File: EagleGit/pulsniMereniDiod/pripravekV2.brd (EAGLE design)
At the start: 80 x 53 mm, 24 parts, among them T1 BD240C, X1 SMKDSP_1,5/2, X2 SMKDSP_1,5/2, X3 SMKDSP_1,5/2, X4 SMKDSP_1,5/6

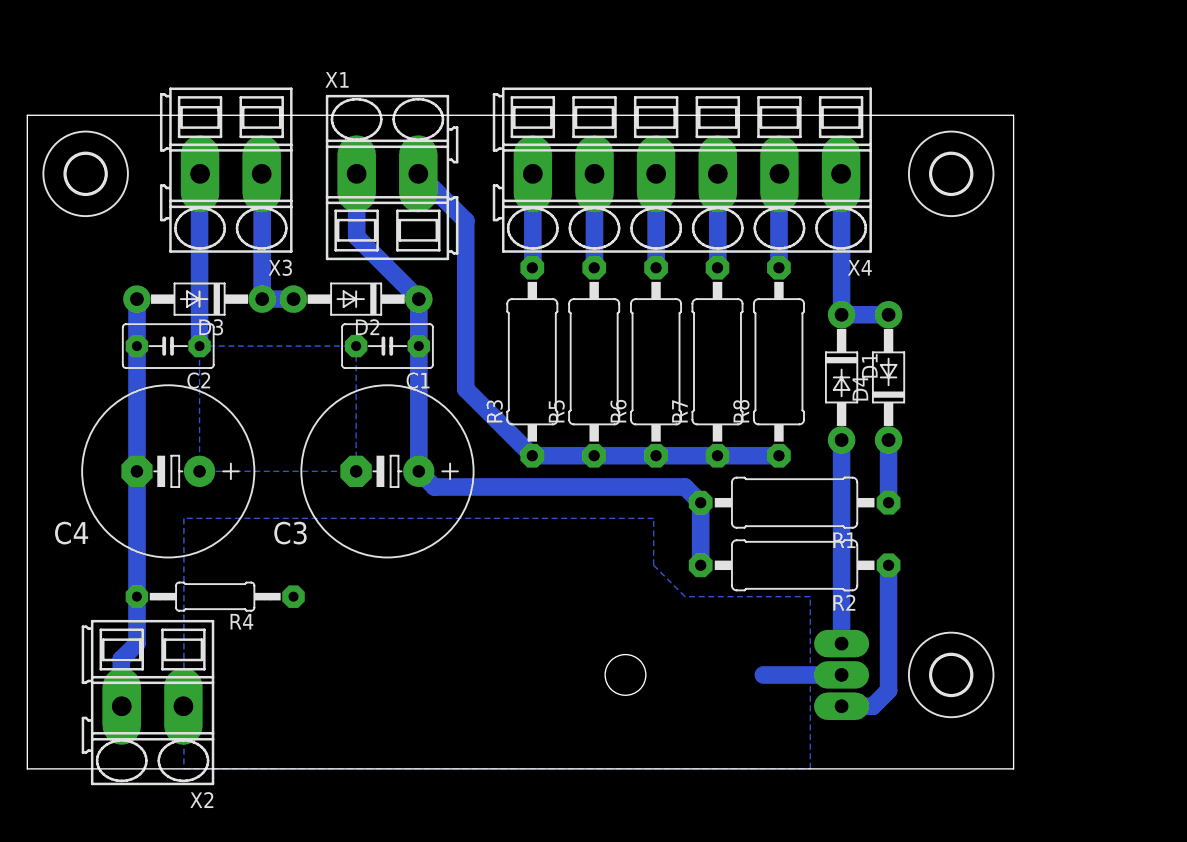
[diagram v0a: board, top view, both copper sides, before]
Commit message: VES: pripravek predelan pro vetsi rozmer rezistoru
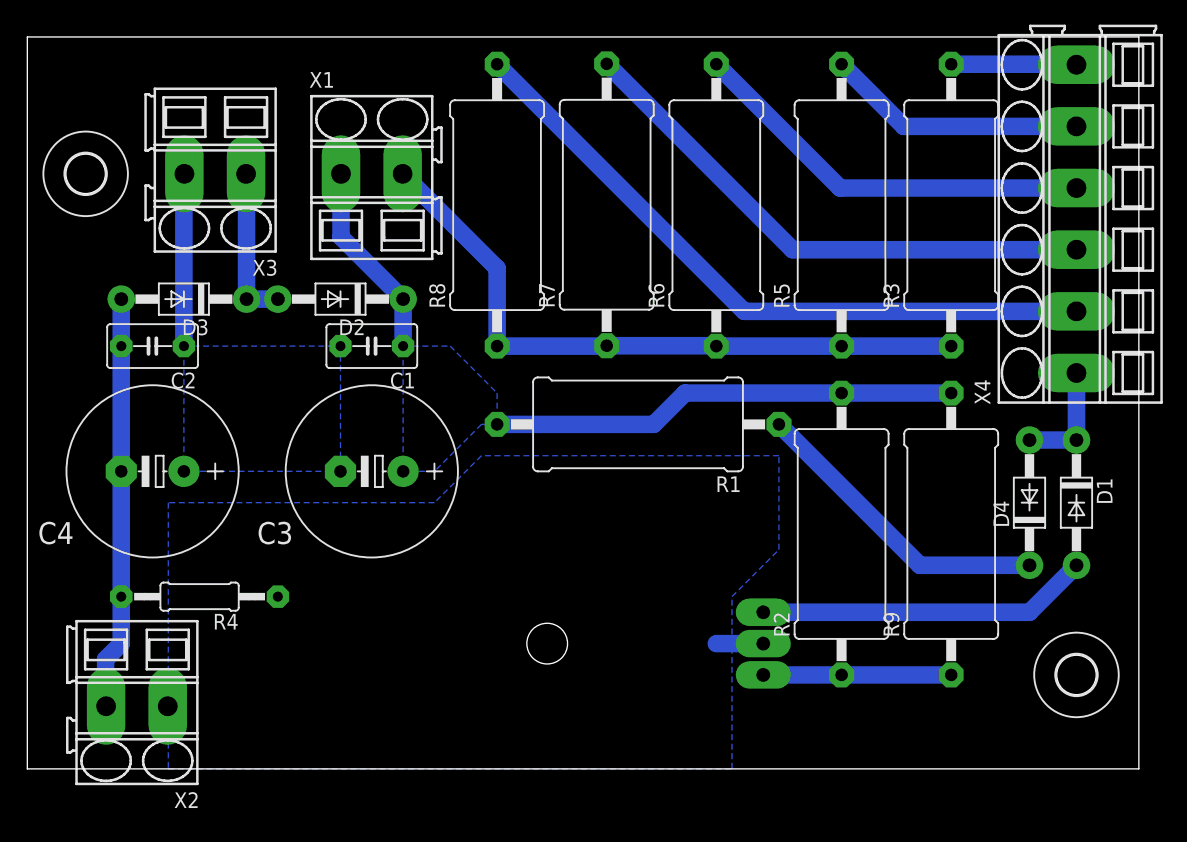
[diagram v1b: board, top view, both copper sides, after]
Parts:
- removed U$1: (no value), holes:3,2
- added R9: 51R, rcl:P0817/22
- R1, R3, R5, R6, R7, R8: device rcl:0411/15 -> rcl:P0817/22
- R2: value 22R -> 51R; device rcl:0411/15 -> rcl:P0817/22
- moved R3 36.3 mm to (74.9, 45.7)
- moved R8 26.2 mm to (38.1, 45.7)
- moved X4 25.5 mm to (85.1, 34.6), turned to 90 degrees
- moved R5 23.7 mm to (66.0, 45.7)
- moved D1 21.6 mm to (85.1, 21.6)
- moved R7 15.6 mm to (47.0, 45.8)
- moved D4 15.3 mm to (81.3, 21.6)
- moved R1 14.2 mm to (49.5, 27.9)
- moved R6 13.6 mm to (55.9, 45.7)
- moved U$2 10.2 mm to (85.1, 7.62)
- moved T1 6.84 mm to (53.3, 10.2)
- moved R2 4.58 mm to (66.0, 19.1), turned to 90 degrees
- moved D2 1.27 mm to (25.4, 38.1)
- moved D3 1.27 mm to (12.7, 38.1)
- moved X3 1.27 mm to (15.2, 48.3)
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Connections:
- net EMITTER: now also R9.1
- net V+: now also R9.2
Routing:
- net N$8: track 7.64 -> 55.3 mm
- net N$6: track 7.62 -> 44.3 mm
- net N$5: track 7.62 -> 33.4 mm
- net N$9: track 5.08 -> 25.1 mm
- net N$3: track 7.62 -> 21.1 mm
- net BASE: track 16.5 -> 27.0 mm
- net N$10: track 46.7 -> 54.0 mm
- net N$4: track 15.3 -> 9.25 mm
- net N$2: track 7.62 -> 10.2 mm
- net COLECTOR: track 6.35 -> 3.81 mm
- net V+: track 55.2 -> 53.9 mm
- net EMITTER: track 14.5 -> 15.2 mm
- added copper zone on layer 16, net V+
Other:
- board size 80 x 53 mm -> 90.2 x 59.4 mm

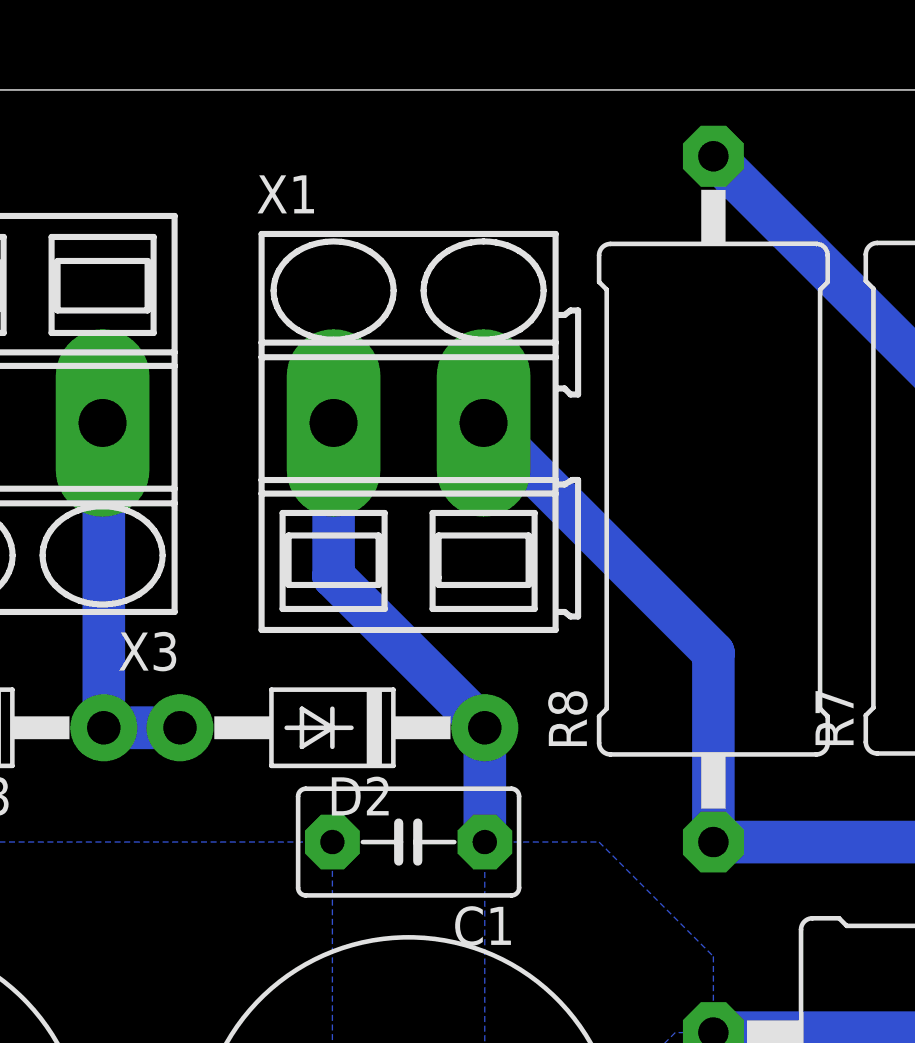
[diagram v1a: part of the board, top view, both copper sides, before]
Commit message: VES: -v pripravku posunuta pozice nekterych soucastek.
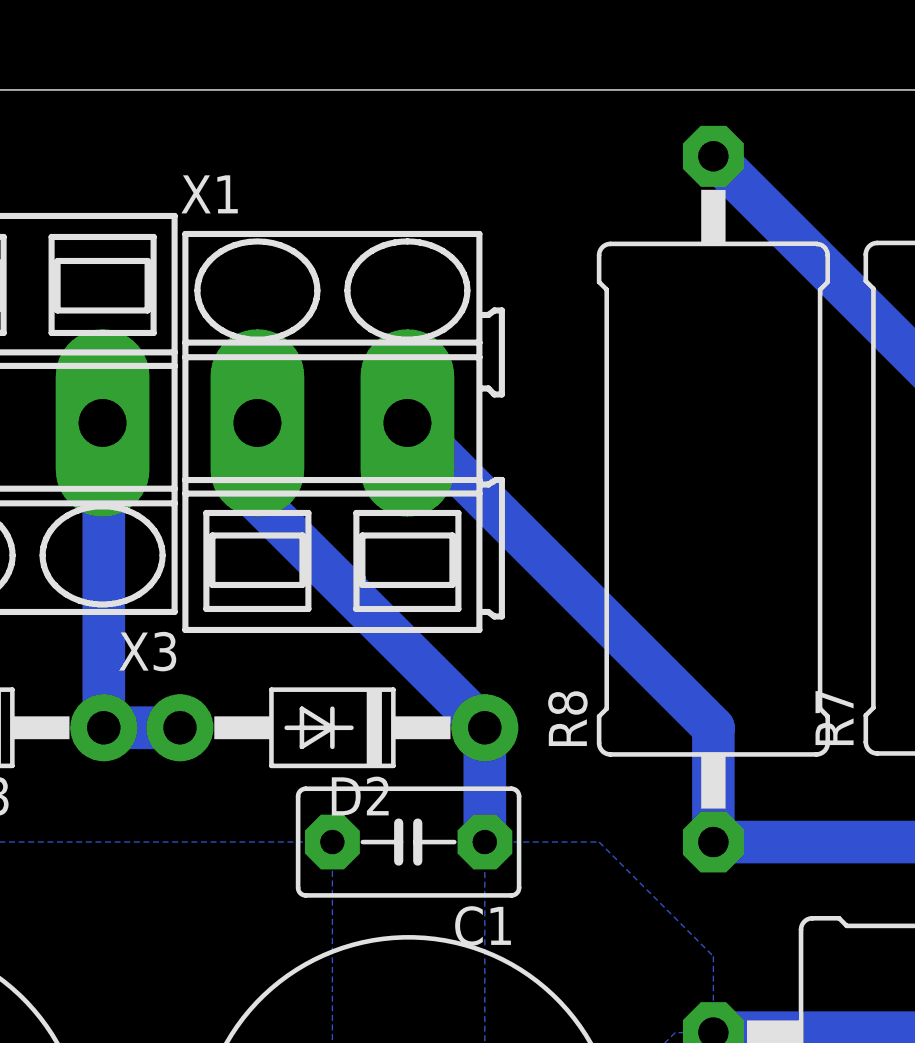
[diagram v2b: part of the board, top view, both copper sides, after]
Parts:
- moved X1 2.54 mm to (25.4, 48.3)
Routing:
- net V+: track 53.9 -> 55.0 mm
- net N$10: track 54.0 -> 55.1 mm
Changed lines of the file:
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@@
 <element name="R8" library="rcl" package="P0817/22" value="68k" x="38.1" y="45.72" rot="R90"/>
 <element name="T1" library="transistor" package="TO220" value="BD240C" x="53.34" y="10.16" rot="MR270"/>
-<element name="X1" library="con-phoenix-smkdsp" package="SMKDSP_1,5/2" value="SMKDSP_1,5/2" x="27.94" y="48.26">
-<attribute name="OC_NEWARK" value="69C8588" x="27.94" y="48.26" size="1.778" layer="27" display="off"/>
-<attribute name="MPN" value="1733570" x="27.94" y="48.26" size="1.778" layer="27" display="off"/>
-<attribute name="MF" value="FARNELL" x="27.94" y="48.26" size="1.778" layer="27" display="off"/>
-<attribute name="OC_FARNELL" value="3041244" x="27.94" y="48.26" size="1.778" layer="27" display="off"/>
+<element name="X1" library="con-phoenix-smkdsp" package="SMKDSP_1,5/2" value="SMKDSP_1,5/2" x="25.4" y="48.26">
+<attribute name="OC_NEWARK" value="69C8588" x="25.4" y="48.26" size="1.778" layer="27" display="off"/>
+<attribute name="MPN" value="1733570" x="25.4" y="48.26" size="1.778" layer="27" display="off"/>
+<attribute name="MF" value="FARNELL" x="25.4" y="48.26" size="1.778" layer="27" display="off"/>
+<attribute name="OC_FARNELL" value="3041244" x="25.4" y="48.26" size="1.778" layer="27" display="off"/>
 </element>
 <element name="X2" library="con-phoenix-smkdsp" package="SMKDSP_1,5/2" value="SMKDSP_1,5/2" x="8.89" y="5.08" rot="R180">
@@
 <contactref element="C3" pad="+"/>
 <contactref element="R1" pad="2"/>
-<wire x1="25.44" y1="48.26" x2="25.44" y2="43.14" width="1.4224" layer="16"/>
-<wire x1="25.44" y1="43.14" x2="30.48" y2="38.1" width="1.4224" layer="16"/>
 <wire x1="30.48" y1="34.29" x2="30.48" y2="38.1" width="1.4224" layer="16"/>
 <contactref element="R9" pad="2"/>
@@
 <vertex x="33.02" y="24.13"/>
 </polygon>
+<wire x1="30.48" y1="38.1" x2="22.86" y2="45.72" width="1.4224" layer="16"/>
+<wire x1="22.86" y1="45.72" x2="22.86" y2="48.22" width="1.4224" layer="16"/>
+<wire x1="22.86" y1="48.22" x2="22.9" y2="48.26" width="1.4224" layer="16"/>
 </signal>
 <signal name="BASE">
@@
 <contactref element="R5" pad="1"/>
 <contactref element="R3" pad="1"/>
-<wire x1="38.1" y1="34.29" x2="38.1" y2="40.6" width="1.4224" layer="16"/>
-<wire x1="38.1" y1="40.6" x2="30.44" y2="48.26" width="1.4224" layer="16"/>
 <wire x1="38.1" y1="34.29" x2="46.95825" y2="34.29" width="1.4224" layer="16"/>
 <wire x1="46.95825" y1="34.29" x2="46.99" y2="34.32175" width="1.4224" layer="16"/>
@@
 <wire x1="55.88" y1="34.29" x2="66.04" y2="34.29" width="1.4224" layer="16"/>
 <wire x1="66.04" y1="34.29" x2="74.93" y2="34.29" width="1.4224" layer="16"/>
+<wire x1="27.9" y1="48.26" x2="27.94" y2="48.26" width="1.4224" layer="16"/>
+<wire x1="27.94" y1="48.26" x2="38.1" y2="38.1" width="1.4224" layer="16"/>
+<wire x1="38.1" y1="38.1" x2="38.1" y2="34.29" width="1.4224" layer="16"/>
 </signal>
 <signal name="N$4">
